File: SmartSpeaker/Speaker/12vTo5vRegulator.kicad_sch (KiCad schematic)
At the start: 7 parts, among them J1 Jack-DC, U3 LM2675N-5

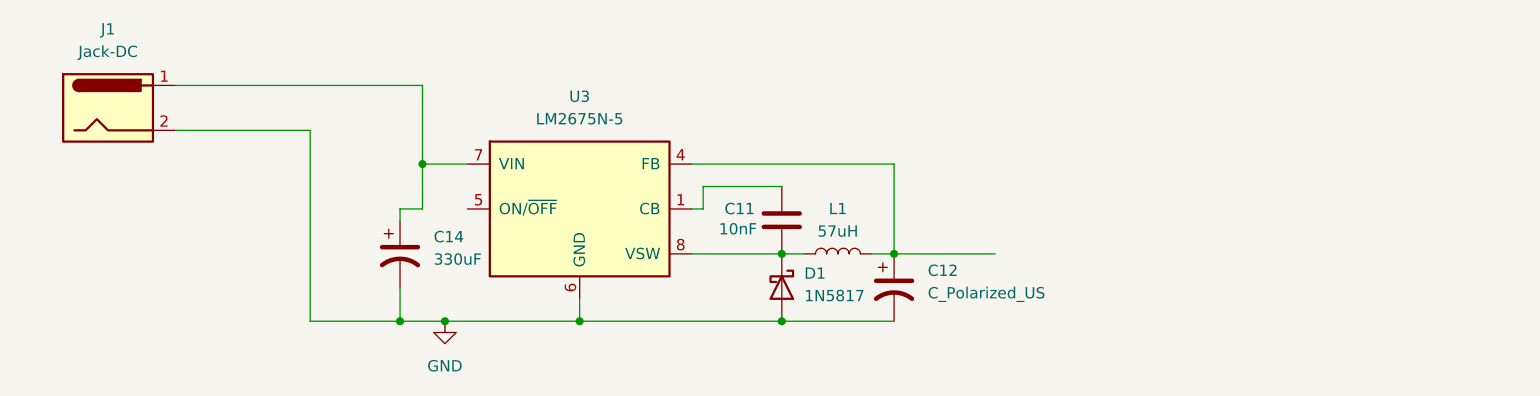
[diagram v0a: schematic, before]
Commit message: add footprints, test points
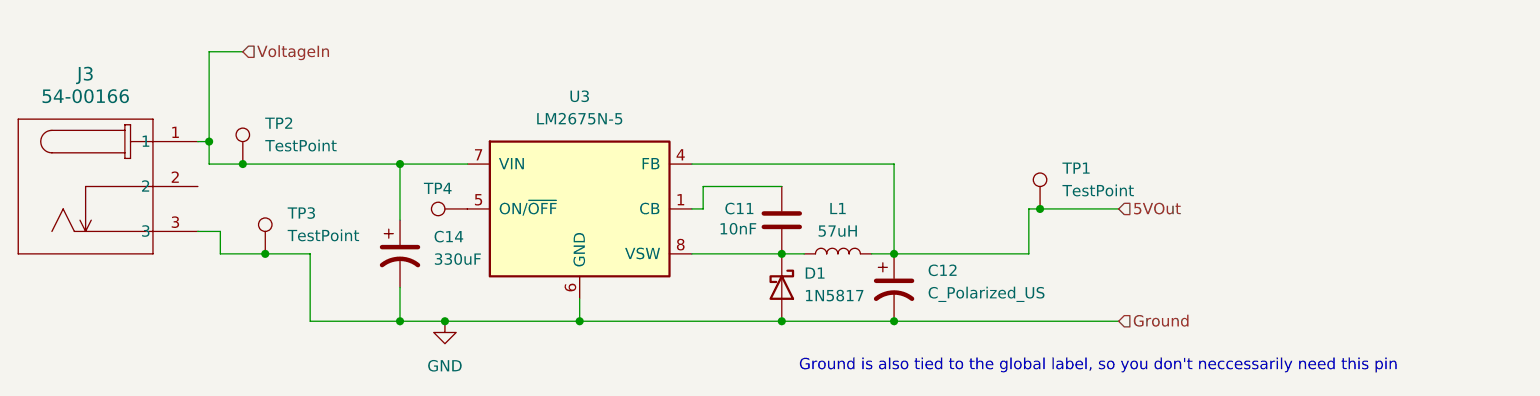
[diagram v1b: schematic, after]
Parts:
- removed J1: Jack-DC, symbol Connector:Jack-DC
- added J3: 54-00166, CONN3_54-00166_TEN, symbol Barrel_Jack_Custom:54-00166
- added TP1, TP2, TP3, TP4: TestPoint, symbol Connector:TestPoint
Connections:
- net GND: now also J3.3, TP3.1
- net 5VOut: now reaches C12.1, L1.2, U3.4 (FB)
- net 5VOut: now also TP1.1
- net VoltageIn: now reaches C14.1, U3.7 (VIN)
- net VoltageIn: now also J3.1, TP2.1
- net at U3.5 (ON/~{OFF}): now also TP4.1
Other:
- note added: "Ground is also tied to the global label, so you don't neccessarily need this pin"

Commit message: add more footprints
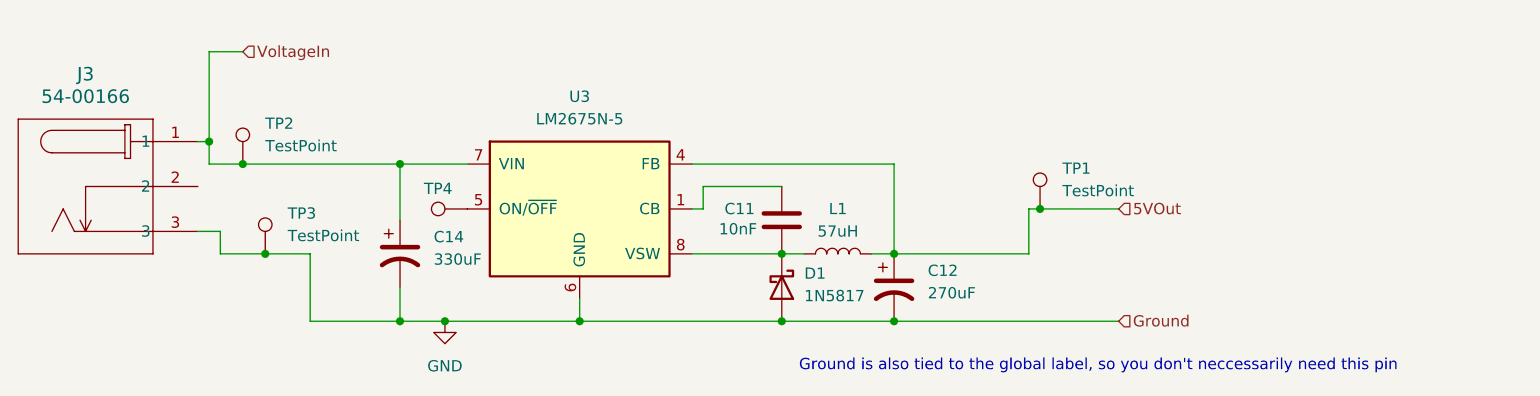
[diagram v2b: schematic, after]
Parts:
- C12: value C_Polarized_US -> 270uF
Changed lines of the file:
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@@
 			)
 		)
-		(property "Value" "C_Polarized_US"
+		(property "Value" "270uF"
 			(at 138.43 88.2649 0)
 			(effects

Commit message: add footprints for test points, jumpers
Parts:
- TP1, TP2, TP3, TP4: footprint (none) -> TestPoint:TestPoint_THTPad_D2.5mm_Drill1.2mm
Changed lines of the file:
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@@
 			)
 		)
-		(property "Footprint" ""
+		(property "Footprint" "TestPoint:TestPoint_THTPad_D2.5mm_Drill1.2mm"
 			(at 66.04 73.66 0)
 			(effects
@@
 			)
 		)
-		(property "Footprint" ""
+		(property "Footprint" "TestPoint:TestPoint_THTPad_D2.5mm_Drill1.2mm"
 			(at 86.36 73.66 0)
 			(effects
@@
 			)
 		)
-		(property "Footprint" ""
+		(property "Footprint" "TestPoint:TestPoint_THTPad_D2.5mm_Drill1.2mm"
 			(at 68.58 83.82 0)
 			(effects
@@
 			)
 		)
-		(property "Footprint" ""
+		(property "Footprint" "TestPoint:TestPoint_THTPad_D2.5mm_Drill1.2mm"
 			(at 156.21 78.74 0)
 			(effects

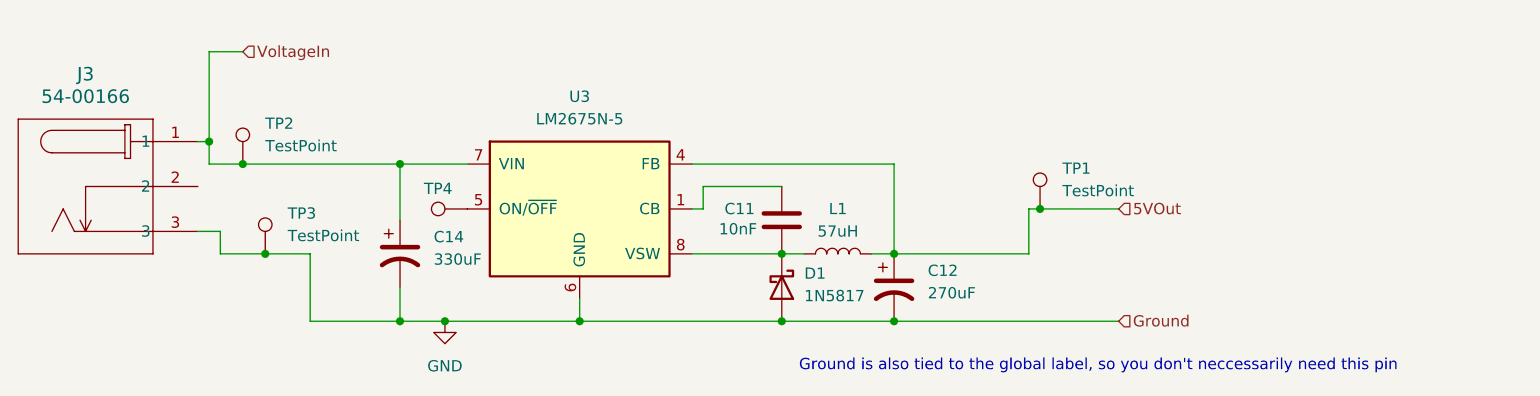
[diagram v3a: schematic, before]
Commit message: Fix some footprint problems, work towards a PCB
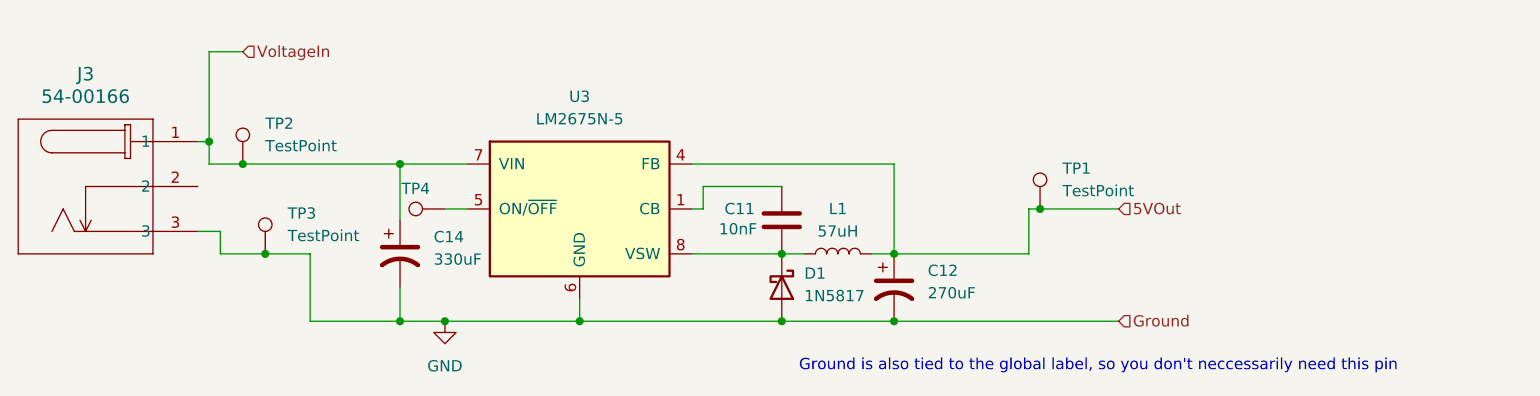
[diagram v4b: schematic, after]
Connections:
- net 5VOut: now also L1.5, L1.6; no longer L1.2
- net at C11.1, D1.1 (K), L1.1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: now also L1.2, L1.3, L1.4
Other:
- moved on the sheet: TP4
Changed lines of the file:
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@@
+	(wire
+		(pts
+			(xy 83.82 78.74) (xy 86.36 78.74)
+		)
+		(stroke
+			(width 0)
+			(type default)
+		)
+	)
 	(wire
 		(pts
@@
 		)
 	)
+	(netclass_flag ""
+		(length 2.54)
+		(shape round)
+		(at 115.57 83.82 180)
+		(fields_autoplaced yes)
+		(effects
+			(font
+				(size 1.27 1.27)
+			)
+			(justify right bottom)
+		)
+		(property "Netclass" "Power"
+			(at 116.2685 86.36 0)
+			(effects
+				(font
+					(size 1.27 1.27)
+					(italic yes)
+				)
+				(justify left)
+			)
+		)
+	)
 	(symbol
 		(lib_id "Device:L")
@@
 		(pin "2"
 		)
+		(pin "4"
+		)
+		(pin "6"
+		)
+		(pin "5"
+		)
+		(pin "3"
+		)
+		(pin "6"
+		)
+		(pin "6"
+		)
 		(instances
 			(project "Speaker"
@@
 	(symbol
 		(lib_id "Connector:TestPoint")
-		(at 86.36 78.74 90)
+		(at 83.82 78.74 90)
 		(unit 1)
 		(exclude_from_sim no)
@@
 		(dnp no)
 		(property "Reference" "TP4"
-			(at 83.058 76.454 90)
+			(at 80.518 76.454 90)
 			(effects
 				(font
@@
 		)
 		(property "Value" "TestPoint"
-			(at 83.058 76.2 90)
+			(at 80.518 76.2 90)
 			(effects
 				(font
@@
 		)
 		(property "Footprint" "TestPoint:TestPoint_THTPad_D2.5mm_Drill1.2mm"
-			(at 86.36 73.66 0)
+			(at 83.82 73.66 0)
 			(effects
 				(font
@@
 		)
 		(property "Datasheet" "~"
-			(at 86.36 73.66 0)
+			(at 83.82 73.66 0)
 			(effects
 				(font
@@
 		)
 		(property "Description" "test point"
-			(at 86.36 78.74 0)
-			(effects
-				(font
+			(at 83.82 78.74 0)
+			(effects
+				(font

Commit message: PCB progress
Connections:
- net 5VOut: now also L1.7, L1.8
- net VSwitch: now reaches C11.1, D1.1 (K), L1.1, L1.2, L1.3, L1.4, U3.8 (VSW)
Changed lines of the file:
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@@
+		)
+	)
+	(label "VSwitch"
+		(at 111.76 83.82 0)
+		(effects
+			(font
+				(size 1.27 1.27)
+			)
+			(justify left bottom)
 		)
 	)
@@
 			)
 			(justify left)
-		)
-	)
-	(netclass_flag ""
-		(length 2.54)
-		(shape round)
-		(at 115.57 83.82 180)
-		(fields_autoplaced yes)
-		(effects
-			(font
-				(size 1.27 1.27)
-			)
-			(justify right bottom)
-		)
-		(property "Netclass" "Power"
-			(at 116.2685 86.36 0)
-			(effects
-				(font
-					(size 1.27 1.27)
-					(italic yes)
-				)
-				(justify left)
-			)
 		)
 	)
@@
 		(pin "3"
 		)
-		(pin "6"
+		(pin "7"
 		)
-		(pin "6"
+		(pin "8"
 		)
 		(instances

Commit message: lots of small improvements
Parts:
- TP1: value TestPoint -> 5Volts
- TP2: value TestPoint -> 24Volts
- TP3: value TestPoint -> Ground
- TP4: value TestPoint -> ON/~{OFF}
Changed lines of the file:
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@@
 			)
 		)
-		(property "Value" "TestPoint"
+		(property "Value" "24Volts"
 			(at 63.5 71.6279 0)
 			(effects
@@
 			)
 		)
-		(property "Value" "TestPoint"
+		(property "Value" "ON/~{OFF}"
 			(at 80.518 76.2 90)
 			(effects
@@
 			)
 		)
-		(property "Value" "TestPoint"
+		(property "Value" "Ground"
 			(at 66.04 81.7879 0)
 			(effects
@@
 			)
 		)
-		(property "Value" "TestPoint"
+		(property "Value" "5Volts"
 			(at 153.67 76.7079 0)
 			(effects

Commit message: updates per wey
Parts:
- J3: footprint CONN3_54-00166_TEN -> BarrelJack:CONN3_54-00166_TEN
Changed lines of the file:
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@@
 			)
 		)
-		(property "Datasheet" "~"
+		(property "Datasheet" "https://www.digikey.com/en/products/detail/schott-corporation/67144080/251676"
 			(at 128.27 83.82 0)
 			(effects
@@
 			)
 		)
-		(property "Footprint" "CONN3_54-00166_TEN"
+		(property "Footprint" "BarrelJack:CONN3_54-00166_TEN"
 			(at 55.88 71.12 0)
 			(effects
